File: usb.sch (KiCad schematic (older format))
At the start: 89 parts, among them J201 USB_B, J202 CONN_ICSP, J203 CONN_MRESET, SW201 SW_RESET, U201 ATmega32U4-AU, U202 MAX7221xWG, Y1 16M

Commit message: LED routing in progress...
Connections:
- net mosi: now also U202.1 (DIN)
- net row1: now also U202.13 (CLK)
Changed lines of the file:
@@
 	0    1    1    0
 $EndComp
+Wire Wire Line
+	8070 4030 7580 4030
+Wire Wire Line
+	8070 4130 7580 4130
+Wire Wire Line
+	8070 4230 7580 4230
 Wire Bus Line
 	3930 2075 3930 2775
 Wire Bus Line
 	3930 3275 3930 3975
+Text Label 7580 4230 0    50   ~ 0
+mosi
+Text Label 7580 4130 0    50   ~ 0
+sck
 $EndSCHEMATC

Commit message: WIP
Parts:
- removed C211: 100n, Capacitor_SMD:C_0805_2012Metric_Pad1.18x1.45mm_HandSolder, symbol Device:C
- added Y201: 16M, Crystal:Crystal_HC49-4H_Vertical, symbol Device:Crystal
- SW201: footprint Button_Switch_THT:SW_PUSH_6mm -> Button_Switch_SMD:SW_SPST_EVPBF
- renumbered Y1 to Y202
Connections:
- net mosi: no longer U202.1 (DIN)
- net row1: no longer U202.13 (CLK)
- net xtal+: now also Y201.1
- net xtal-: now also Y201.2
- net soft_ss: now reaches U201.39 (PF4)
- net soft_ss: now also U202.12 (~CS)
- net soft_sck: now reaches U201.40 (PF1)
- net soft_sck: now also U202.13 (CLK)
- net soft_mosi: now reaches U201.41 (PF0)
- net soft_mosi: now also U202.1 (DIN)
- no-connect marks 10 -> 7
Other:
- note added: "THT XTAL"
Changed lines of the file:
@@
 Sheet 2 2
 Title "Mechboard16"
-Date "2023-11-25"
+Date "2023-11-26"
 Rev "1git"
 Comp "SukkoPera"
@@
 F 0 "SW201" H 1445 2460 50  0000 C CNN
 F 1 "SW_RESET" H 1445 2369 50  0000 C CNN
-F 2 "Button_Switch_THT:SW_PUSH_6mm" H 1445 2375 50  0001 C CNN
+F 2 "Button_Switch_SMD:SW_SPST_EVPBF" H 1445 2375 50  0001 C CNN
 F 3 "~" H 1445 2375 50  0001 C CNN
 F 4 "C410365" H 1445 2175 50  0001 C CNN "LCSC"
@@
 Connection ~ 14260 7680
 Connection ~ 14260 8270
-$Comp
-L Device:C C211
-U 1 1 5FBB40D6
-P 15175 7975
-F 0 "C211" H 15290 8021 50  0000 L CNN
-F 1 "100n" H 15290 7930 50  0000 L CNN
-F 2 "Capacitor_SMD:C_0805_2012Metric_Pad1.18x1.45mm_HandSolder" H 15213 7825 50  0001 C CNN
-F 3 "~" H 15175 7975 50  0001 C CNN
-F 4 "C49678" H 15175 7975 50  0001 C CNN "LCSC"
-	1    15175 7975
-	1    0    0    -1
-$EndComp
-Wire Wire Line
-	15175 7680 15175 7825
-Wire Wire Line
-	15175 8270 15175 8125
 Wire Wire Line
 	2610 5575 2660 5575
@@
 Wire Wire Line
 	2660 5575 2710 5575
-Connection ~ 14720 7680
-Wire Wire Line
-	14720 7680 15175 7680
-Connection ~ 14720 8270
-Wire Wire Line
-	14720 8270 15175 8270
 Text Notes 14275 7475 0    50   ~ 0
 DECOUPLING
@@
 INT6
 $Comp
-L Device:Crystal_GND24 Y1
+L Device:Crystal_GND24 Y202
 U 1 1 613F6F1B
 P 1860 2480
-F 0 "Y1" V 1910 2625 50  0000 L CNN
+F 0 "Y202" V 1910 2625 50  0000 L CNN
 F 1 "16M" V 1860 2405 50  0000 L CNN
 F 2 "Crystal:Crystal_SMD_3225-4Pin_3.2x2.5mm" H 1860 2480 50  0001 C CNN
@@
 NoConn ~ 3310 4275
 NoConn ~ 3310 4375
-NoConn ~ 3310 4575
-NoConn ~ 3310 4675
-NoConn ~ 3310 4775
 NoConn ~ 3310 4875
 NoConn ~ 3310 4975
@@
 Wire Wire Line
 	8070 4230 7580 4230
+Text Label 7580 4230 0    50   ~ 0
+soft_mosi
+Text Label 7580 4130 0    50   ~ 0
+soft_sck
+Wire Wire Line
+	3310 4575 3830 4575
+Text Label 3830 4575 2    50   ~ 0
+soft_mosi
+Wire Wire Line
+	3310 4675 3830 4675
+Wire Wire Line
+	3310 4775 3830 4775
+Text Label 3830 4675 2    50   ~ 0
+soft_sck
+Text Label 3830 4775 2    50   ~ 0
+soft_ss
+Text Label 7580 4030 0    50   ~ 0
+soft_ss
+$Comp
+L Device:Crystal Y201
+U 1 1 6701DCCD
+P 695 2480
+F 0 "Y201" V 649 2611 50  0000 L CNN
+F 1 "16M" V 740 2611 50  0000 L CNN
+F 2 "Crystal:Crystal_HC49-4H_Vertical" H 695 2480 50  0001 C CNN
+F 3 "~" H 695 2480 50  0001 C CNN
+	1    695  2480
+	0    1    1    0
+$EndComp
+Wire Wire Line
+	695  2330 695  2275
+Wire Wire Line
+	695  2275 900  2275
+Wire Wire Line
+	695  2630 695  2695
+Wire Wire Line
+	695  2695 905  2695
+Text Label 900  2275 2    50   ~ 0
+xtal+
+Text Label 905  2695 2    50   ~ 0
+xtal-
+Text Notes 615  2825 0    50   ~ 0
+THT XTAL
 Wire Bus Line
 	3930 2075 3930 2775
 Wire Bus Line
 	3930 3275 3930 3975
-Text Label 7580 4230 0    50   ~ 0
-mosi
-Text Label 7580 4130 0    50   ~ 0
-sck
 $EndSCHEMATC

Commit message: WIP2
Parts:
- U202: value MAX7221xWG -> MAX7221
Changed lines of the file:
@@
 P 8470 3430
 F 0 "U202" H 8695 4390 50  0000 C CNN
-F 1 "MAX7221xWG" H 8780 2475 50  0000 C CNN
+F 1 "MAX7221" H 8780 2475 50  0000 C CNN
 F 2 "Package_SO:SOIC-24W_7.5x15.4mm_P1.27mm" H 8420 3480 50  0001 C CNN
 F 3 "https://datasheets.maximintegrated.com/en/ds/MAX7219-MAX7221.pdf" H 8520 3280 50  0001 C CNN

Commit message: I'm tired and I want to go to bed
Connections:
- net soft_mosi: now also U201.40 (PF1); no longer U201.41 (PF0)
- net soft_sck: now also U201.39 (PF4); no longer U201.40 (PF1)
- net soft_ss: now also U201.41 (PF0); no longer U201.39 (PF4)
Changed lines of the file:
@@
 Wire Wire Line
 	3310 4575 3830 4575
-Text Label 3830 4575 2    50   ~ 0
+Text Label 3830 4675 2    50   ~ 0
 soft_mosi
 Wire Wire Line
@@
 Wire Wire Line
 	3310 4775 3830 4775
-Text Label 3830 4675 2    50   ~ 0
+Text Label 3830 4775 2    50   ~ 0
 soft_sck
-Text Label 3830 4775 2    50   ~ 0
+Text Label 3830 4575 2    50   ~ 0
 soft_ss
 Text Label 7580 4030 0    50   ~ 0

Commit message: I need to drink more than you seem to think
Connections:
- net soft_mosi: now also U201.39 (PF4); no longer U201.40 (PF1)
- net soft_sck: now also U201.38 (PF5); no longer U201.39 (PF4)
- net soft_ss: now also U201.40 (PF1); no longer U201.41 (PF0)
- net ~mreset: now also U201.41 (PF0); no longer U201.31 (PC6)
- no-connect marks 7 -> 6
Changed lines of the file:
@@
 	3310 3175 4575 3175
 Wire Wire Line
-	3310 3075 3830 3075
-Text Label 3830 3075 2    50   ~ 0
+	3310 4575 3830 4575
+Text Label 3830 4575 2    50   ~ 0
 ~mreset
 NoConn ~ 3310 4275
 NoConn ~ 3310 4375
-NoConn ~ 3310 4875
 NoConn ~ 3310 4975
 NoConn ~ 3310 5075
@@
 soft_sck
 Wire Wire Line
-	3310 4575 3830 4575
+	3310 4675 3830 4675
+Text Label 3830 4775 2    50   ~ 0
+soft_mosi
+Wire Wire Line
+	3310 4775 3830 4775
+Wire Wire Line
+	3310 4875 3830 4875
+Text Label 3830 4875 2    50   ~ 0
+soft_sck
 Text Label 3830 4675 2    50   ~ 0
-soft_mosi
-Wire Wire Line
-	3310 4675 3830 4675
-Wire Wire Line
-	3310 4775 3830 4775
-Text Label 3830 4775 2    50   ~ 0
-soft_sck
-Text Label 3830 4575 2    50   ~ 0
 soft_ss
 Text Label 7580 4030 0    50   ~ 0

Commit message: HEEEEEAAAADLOOOOOOOOOOONGGG!
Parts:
- removed LD201: STATUS_LED, LED_SMD:LED_0805_2012Metric_Pad1.15x1.40mm_HandSolder, symbol Device:LED
- added C211: 100n, Capacitor_SMD:C_0805_2012Metric_Pad1.18x1.45mm_HandSolder, symbol Device:C
- added J204: CONN_LED, Connector_PinHeader_2.54mm:PinHeader_1x04_P2.54mm_Vertical, symbol Connector:Conn_01x04_Male
- added R205, R206: 1k, Resistor_SMD:R_0805_2012Metric_Pad1.20x1.40mm_HandSolder, symbol Device:R
- C203: footprint Capacitor_Tantalum_SMD:CP_EIA-3528-21_Kemet-B_Pad1.50x2.35mm_HandSolder -> Capacitor_THT:CP_Radial_D6.3mm_P2.50mm
- C204: footprint Capacitor_SMD:C_1206_3216Metric_Pad1.33x1.80mm_HandSolder -> Capacitor_THT:CP_Radial_D5.0mm_P2.00mm
- renumbered R205 to R207
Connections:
- net +5V: now also C211.1
- net GND: now also C211.2, J204.1 (Pin_1); no longer R204.2
- net soft_mosi: now also U201.37 (PF6); no longer U201.39 (PF4)
- net soft_sck: now also U201.36 (PF7); no longer U201.38 (PF5)
- net soft_ss: now also U201.38 (PF5); no longer U201.40 (PF1)
- net ~mreset: now also U201.31 (PC6); no longer U201.41 (PF0)
- net at R204.1: now also J204.2 (Pin_2)
- net st_led: no longer names the net of U201.32 (PC7)
- new net: J204.3 (Pin_3), R205.1
- new net: J204.4 (Pin_4), R206.1
- new net st_le_b: R206.2, U201.39 (PF4)
- new net st_led_g: R205.2, U201.40 (PF1)
- new net st_led_r: R204.2, U201.41 (PF0)
- no-connect marks 6 -> 5
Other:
- moved on the sheet: R204
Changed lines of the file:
@@
 U 1 1 5E5DEAA1
 P 2020 1940
-F 0 "R201" H 2075 1940 50  0000 L CNN
-F 1 "10k" V 2020 1870 50  0000 L CNN
+F 0 "R201" H 1951 1986 50  0000 R CNN
+F 1 "10k" H 1951 1895 50  0000 R CNN
 F 2 "Resistor_SMD:R_0805_2012Metric_Pad1.20x1.40mm_HandSolder" V 1950 1940 50  0001 C CNN
 F 3 "~" H 2020 1940 50  0001 C CNN
@@
 U 1 1 5E6516EC
 P 6280 2815
-F 0 "R202" V 6095 2815 50  0000 C CNN
-F 1 "22" V 6195 2815 50  0000 C CNN
+F 0 "R202" V 6073 2815 50  0000 C CNN
+F 1 "22" V 6164 2815 50  0000 C CNN
 F 2 "Resistor_SMD:R_0805_2012Metric_Pad1.20x1.40mm_HandSolder" V 6210 2815 50  0001 C CNN
 F 3 "~" H 6280 2815 50  0001 C CNN
@@
 Wire Wire Line
 	1645 2175 2020 2175
-$Comp
-L Device:LED LD201
-U 1 1 5E6BFF28
-P 4725 3175
-F 0 "LD201" H 4920 3130 50  0000 C CNN
-F 1 "STATUS_LED" H 4725 3280 50  0000 C CNN
-F 2 "LED_SMD:LED_0805_2012Metric_Pad1.15x1.40mm_HandSolder" H 4725 3175 50  0001 C CNN
-F 3 "~" H 4725 3175 50  0001 C CNN
-F 4 "C2297" H 4725 3175 50  0001 C CNN "LCSC"
-	1    4725 3175
-	-1   0    0    1
-$EndComp
-$Comp
-L Device:R R204
-U 1 1 5E6C78E0
-P 5040 3395
-F 0 "R204" H 5095 3395 50  0000 L CNN
-F 1 "1k" V 5040 3350 50  0000 L CNN
-F 2 "Resistor_SMD:R_0805_2012Metric_Pad1.20x1.40mm_HandSolder" V 4970 3395 50  0001 C CNN
-F 3 "~" H 5040 3395 50  0001 C CNN
-F 4 "C17513" H 5040 3395 50  0001 C CNN "LCSC"
-	1    5040 3395
-	1    0    0    -1
-$EndComp
-Wire Wire Line
-	4875 3175 5040 3175
-Wire Wire Line
-	5040 3175 5040 3245
-$Comp
-L power:GND #PWR016
-U 1 1 5E6CD612
-P 5040 3630
-F 0 "#PWR016" H 5040 3380 50  0001 C CNN
-F 1 "GND" H 5045 3457 50  0000 C CNN
-F 2 "" H 5040 3630 50  0001 C CNN
-F 3 "" H 5040 3630 50  0001 C CNN
-	1    5040 3630
-	1    0    0    -1
-$EndComp
-Wire Wire Line
-	5040 3545 5040 3630
 $Comp
 L Connector_Generic:Conn_02x03_Odd_Even J202
@@
 	1565 2975 1565 3035
 Connection ~ 1565 2975
-Text Label 3830 3175 2    50   ~ 0
-st_led
 Text Label 1820 2330 0    50   ~ 0
 xtal+
@@
 F 0 "C203" H 1450 3231 50  0000 R CNN
 F 1 "100u" H 1450 3140 50  0000 R CNN
-F 2 "Capacitor_Tantalum_SMD:CP_EIA-3528-21_Kemet-B_Pad1.50x2.35mm_HandSolder" H 1565 3185 50  0001 C CNN
+F 2 "Capacitor_THT:CP_Radial_D6.3mm_P2.50mm" H 1565 3185 50  0001 C CNN
 F 3 "~" H 1565 3185 50  0001 C CNN
 F 4 "C16133" H 1565 3185 50  0001 C CNN "LCSC"
@@
 F 0 "C204" H 1900 3816 50  0000 L CNN
 F 1 "1u" H 1900 3725 50  0000 L CNN
-F 2 "Capacitor_SMD:C_1206_3216Metric_Pad1.33x1.80mm_HandSolder" H 1823 3620 50  0001 C CNN
+F 2 "Capacitor_THT:CP_Radial_D5.0mm_P2.00mm" H 1823 3620 50  0001 C CNN
 F 3 "~" H 1785 3770 50  0001 C CNN
 F 4 "C1848" H 1785 3770 50  0001 C CNN "LCSC"
@@
 	3930 3275 4035 3275
 Wire Wire Line
-	3310 3175 4575 3175
-Wire Wire Line
-	3310 4575 3830 4575
-Text Label 3830 4575 2    50   ~ 0
+	3310 4775 4010 4775
+Wire Wire Line
+	3310 3075 3830 3075
+Text Label 3830 3075 2    50   ~ 0
 ~mreset
 NoConn ~ 3310 4275
 NoConn ~ 3310 4375
-NoConn ~ 3310 4975
-NoConn ~ 3310 5075
 $Comp
 L power:+5V #PWR0201
@@
 $EndComp
 $Comp
-L Device:R R205
+L Device:R R207
 U 1 1 66613A96
 P 7920 2395
-F 0 "R205" H 7850 2441 50  0000 R CNN
+F 0 "R207" H 7850 2441 50  0000 R CNN
 F 1 "TBD" H 7850 2350 50  0000 R CNN
 F 2 "Resistor_SMD:R_0805_2012Metric_Pad1.20x1.40mm_HandSolder" V 7850 2395 50  0001 C CNN
@@
 soft_sck
 Wire Wire Line
-	3310 4675 3830 4675
-Text Label 3830 4775 2    50   ~ 0
+	3310 4875 3830 4875
+Text Label 3830 4975 2    50   ~ 0
 soft_mosi
 Wire Wire Line
-	3310 4775 3830 4775
-Wire Wire Line
-	3310 4875 3830 4875
+	3310 4975 3830 4975
+Wire Wire Line
+	3310 5075 3830 5075
+Text Label 3830 5075 2    50   ~ 0
+soft_sck
 Text Label 3830 4875 2    50   ~ 0
-soft_sck
-Text Label 3830 4675 2    50   ~ 0
 soft_ss
 Text Label 7580 4030 0    50   ~ 0
@@
 Text Notes 615  2825 0    50   ~ 0
 THT XTAL
+Text Label 3830 4675 2    50   ~ 0
+st_led_g
+Wire Wire Line
+	3310 4675 4010 4675
+Wire Wire Line
+	3310 4575 4010 4575
+$Comp
+L Connector:Conn_01x04_Male J204
+U 1 1 65CBEB83
+P 4775 4575
+F 0 "J204" H 4747 4549 50  0000 R CNN
+F 1 "CONN_LED" H 4747 4458 50  0000 R CNN
+F 2 "Connector_PinHeader_2.54mm:PinHeader_1x04_P2.54mm_Vertical" H 4775 4575 50  0001 C CNN
+F 3 "~" H 4775 4575 50  0001 C CNN
+	1    4775 4575
+	-1   0    0    -1
+$EndComp
+$Comp
+L power:GND #PWR016
+U 1 1 5E6CD612
+P 4505 5030
+F 0 "#PWR016" H 4505 4780 50  0001 C CNN
+F 1 "GND" H 4510 4857 50  0000 C CNN
+F 2 "" H 4505 5030 50  0001 C CNN
+F 3 "" H 4505 5030 50  0001 C CNN
+	1    4505 5030
+	-1   0    0    -1
+$EndComp
+Wire Wire Line
+	4310 4575 4575 4575
+Wire Wire Line
+	4310 4675 4575 4675
+Wire Wire Line
+	4310 4775 4575 4775
+$Comp
+L Device:R R205
+U 1 1 65D6EB57
+P 4160 4675
+F 0 "R205" V 4195 4460 50  0000 C CNN
+F 1 "1k" V 4200 4835 50  0000 C CNN
+F 2 "Resistor_SMD:R_0805_2012Metric_Pad1.20x1.40mm_HandSolder" V 4090 4675 50  0001 C CNN
+F 3 "~" H 4160 4675 50  0001 C CNN
+F 4 "C17513" H 4160 4675 50  0001 C CNN "LCSC"
+	1    4160 4675
+	0    1    -1   0
+$EndComp
+NoConn ~ 3310 3175
+Text Label 3830 4775 2    50   ~ 0
+st_le_b
+Text Label 3830 4575 2    50   ~ 0
+st_led_r
+$Comp
+L Device:R R204
+U 1 1 5E6C78E0
+P 4160 4575
+F 0 "R204" V 4195 4360 50  0000 C CNN
+F 1 "1k" V 4200 4735 50  0000 C CNN
+F 2 "Resistor_SMD:R_0805_2012Metric_Pad1.20x1.40mm_HandSolder" V 4090 4575 50  0001 C CNN
+F 3 "~" H 4160 4575 50  0001 C CNN
+F 4 "C17513" H 4160 4575 50  0001 C CNN "LCSC"
+	1    4160 4575
+	0    1    -1   0
+$EndComp
+$Comp
+L Device:R R206
+U 1 1 65D6F2CC
+P 4160 4775
+F 0 "R206" V 4195 4560 50  0000 C CNN
+F 1 "1k" V 4200 4935 50  0000 C CNN
+F 2 "Resistor_SMD:R_0805_2012Metric_Pad1.20x1.40mm_HandSolder" V 4090 4775 50  0001 C CNN
+F 3 "~" H 4160 4775 50  0001 C CNN
+F 4 "C17513" H 4160 4775 50  0001 C CNN "LCSC"
+	1    4160 4775
+	0    1    -1   0
+$EndComp
+Wire Wire Line
+	4505 4475 4575 4475
+Wire Wire Line
+	4505 4475 4505 5030
+$Comp
+L Device:C C211
+U 1 1 65B66DA3
+P 15180 7975
+F 0 "C211" H 15295 8021 50  0000 L CNN
+F 1 "100n" H 15295 7930 50  0000 L CNN
+F 2 "Capacitor_SMD:C_0805_2012Metric_Pad1.18x1.45mm_HandSolder" H 15218 7825 50  0001 C CNN
+F 3 "~" H 15180 7975 50  0001 C CNN
+F 4 "C49678" H 15180 7975 50  0001 C CNN "LCSC"
+	1    15180 7975
+	1    0    0    -1
+$EndComp
+Wire Wire Line
+	15180 7680 15180 7825
+Wire Wire Line
+	15180 8270 15180 8125
+Wire Wire Line
+	14720 7680 15180 7680
+Wire Wire Line
+	14720 8270 15180 8270
+Connection ~ 14720 7680
+Connection ~ 14720 8270
 Wire Bus Line
 	3930 2075 3930 2775

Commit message: Done! Just some finishing touches left...
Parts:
- U202: LCSC (none) -> C124668
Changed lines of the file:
@@
 F 2 "Package_SO:SOIC-24W_7.5x15.4mm_P1.27mm" H 8420 3480 50  0001 C CNN
 F 3 "https://datasheets.maximintegrated.com/en/ds/MAX7219-MAX7221.pdf" H 8520 3280 50  0001 C CNN
+F 4 "C124668" H 8470 3430 50  0000 C CNN "LCSC"
 	1    8470 3430
 	1    0    0    -1
@@
 Wire Wire Line
 	4505 4475 4505 5030
+Wire Wire Line
+	15180 7680 15180 7825
+Wire Wire Line
+	15180 8270 15180 8125
+Wire Wire Line
+	14720 7680 15180 7680
+Wire Wire Line
+	14720 8270 15180 8270
+Connection ~ 14720 7680
+Connection ~ 14720 8270
+Wire Bus Line
+	3930 2075 3930 2775
+Wire Bus Line
+	3930 3275 3930 3975
 $Comp
 L Device:C C211
@@
 	1    0    0    -1
 $EndComp
-Wire Wire Line
-	15180 7680 15180 7825
-Wire Wire Line
-	15180 8270 15180 8125
-Wire Wire Line
-	14720 7680 15180 7680
-Wire Wire Line
-	14720 8270 15180 8270
-Connection ~ 14720 7680
-Connection ~ 14720 8270
-Wire Bus Line
-	3930 2075 3930 2775
-Wire Bus Line
-	3930 3275 3930 3975
 $EndSCHEMATC

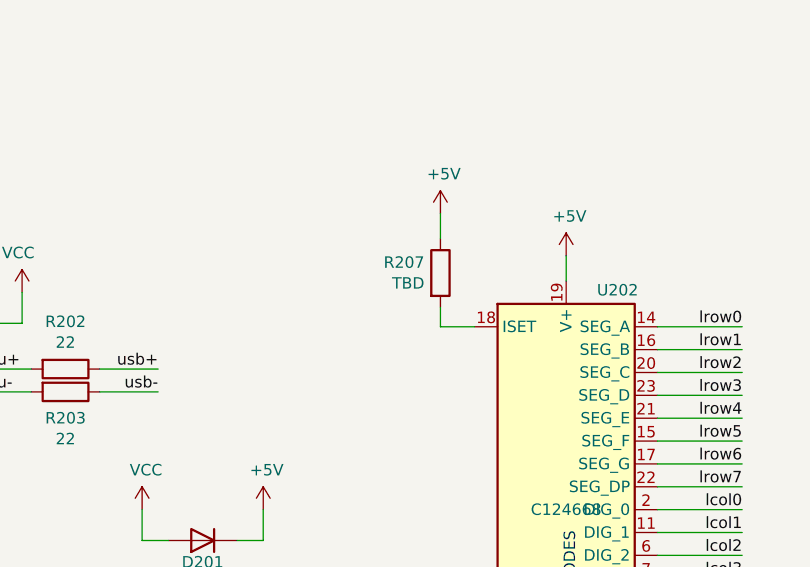
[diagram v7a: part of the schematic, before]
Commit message: Add legend on J204
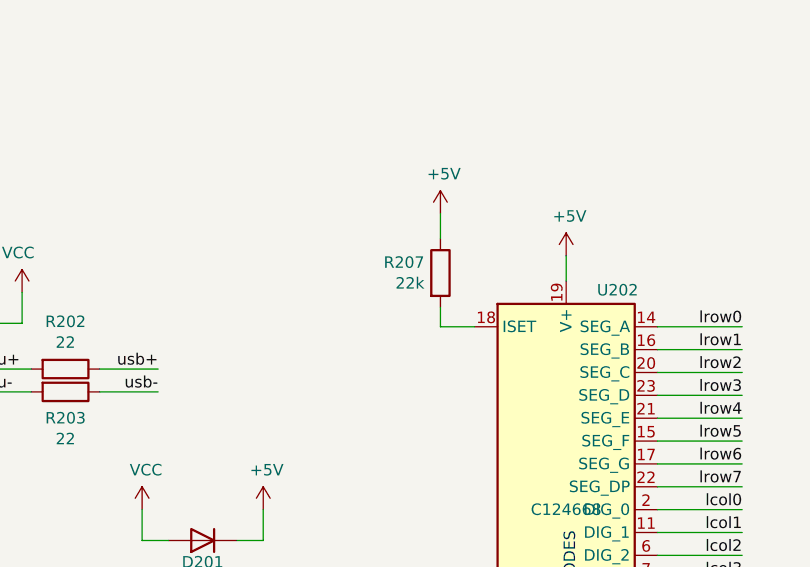
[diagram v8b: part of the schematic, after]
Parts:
- R207: value TBD -> 22k
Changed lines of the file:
@@
 P 7920 2395
 F 0 "R207" H 7850 2441 50  0000 R CNN
-F 1 "TBD" H 7850 2350 50  0000 R CNN
+F 1 "22k" H 7850 2350 50  0000 R CNN
 F 2 "Resistor_SMD:R_0805_2012Metric_Pad1.20x1.40mm_HandSolder" V 7850 2395 50  0001 C CNN
 F 3 "~" H 7920 2395 50  0001 C CNN
